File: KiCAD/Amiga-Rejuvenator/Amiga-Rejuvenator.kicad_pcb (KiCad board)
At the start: 4 copper layers, 241.8 x 174.8 mm, 121 parts, among them J1 VIA, J15 28M, J17 RMBCLKS, J18 GND, J19 +12X, U1 74LS245, U10 V53C104, U11 V53C104, U12 V53C104, U13 V53C104, U14 74LS244-U16,U17, U15 74LS373, U16 74LS244-U16,U17, U17 74LS244-U16,U17, U18 512K-ROM, U19 8372-FatAgnus, U19B1 8361-Agnus, U2 74LS393-U2, U20 8364-Paula, U20B1 8364-Paula, U21 74LS245, U22 74LS245, U23 RP, U24 RP, U25 8362-Denise, U25B1 8362-Denise, U26 74HC245, U27 OKI6242B, U28 PAL16L8, U29 PAL16L8, U3 74F257, U30 PAL20L8, U31 PAL20L8, U32 74LS74, U33 74LS04, U34 74HC245, U35 74F257, U36 PALCAS, U37 PALEN, U38 U3I 244, U39 U3G 244, U4 74LS244-U16,U17, U40 U2J F257, U41 U2I F257, U5 74LS373, U6 V53C104, U7 V53C104, U8 V53C104, U9 V53C104, X1 X1, X14 X14, X15 X15, X16 VideoSlot 1, X17 VideoSlot 2, Y1 Crystal

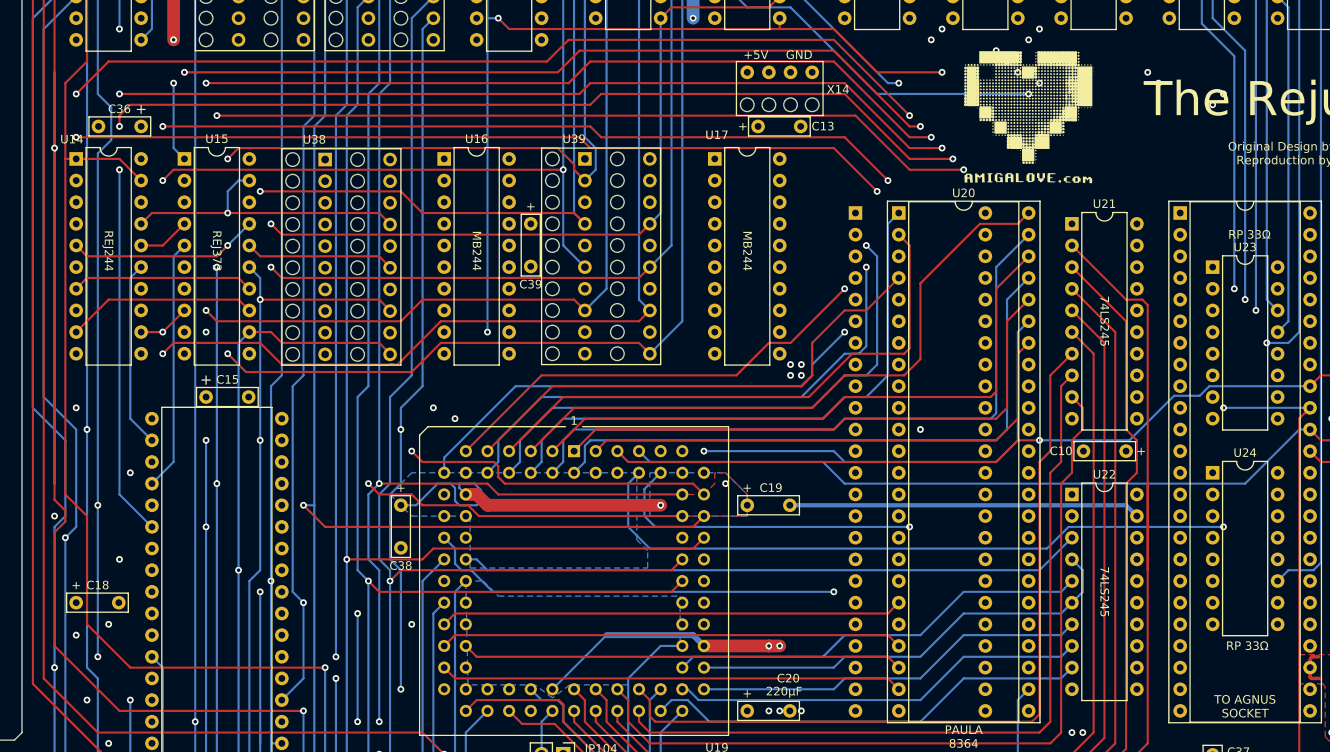
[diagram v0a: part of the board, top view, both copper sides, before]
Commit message: Signal name updates
Signal name updates on KiCAD schematics and board artwork.
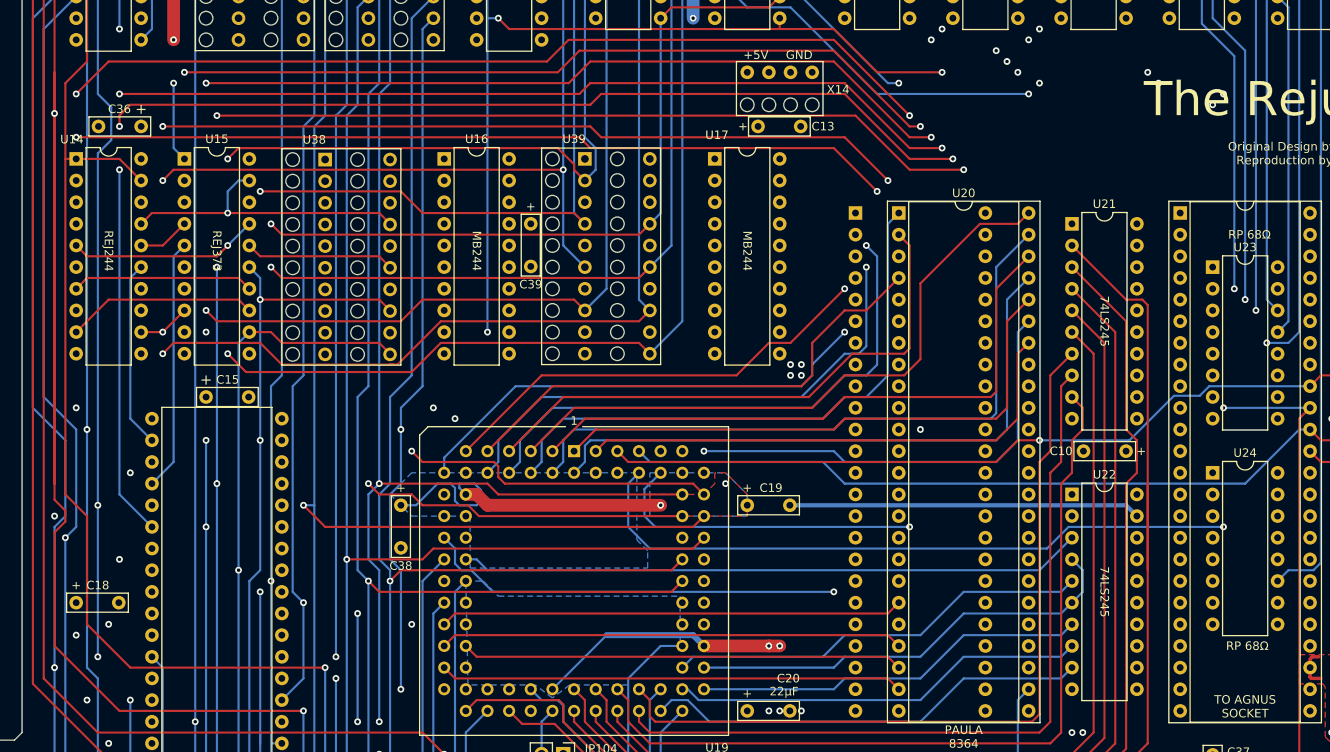
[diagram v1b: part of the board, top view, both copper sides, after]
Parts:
- removed G***: LOGO, rejuvenator_positions:Untitled
- J1: value VIA -> GND
- JP102: value MEM_CONFIG -> JUMPERS
- R10, R11, R12, R6, R7, R9: value 47 -> 33
- U38: value U3I 244 -> U3I
- U39: value U3G 244 -> U3G
- U40: value U2J F257 -> U2J
- U41: value U2I F257 -> U2I
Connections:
- net /REJ.1 renamed /REJ1
- net /REJ.2 renamed /REJ2
- net /REJ.3 renamed /REJ3
- net /REJ.4 renamed /~CNT
- net /REJ.KICK renamed /REJKICK
- net /REJ.MCFG1 renamed /MCFG1
- net /REJ.MCFG2 renamed /MCFG2
- net /REJ.~CE renamed /~DAE
- net /REJ.~OE1 renamed /~CDRREJ
- net /REJ.~OE2 renamed /~CDWREJ
- net /RTC.~RD renamed /~CLKR
- net /RTC.~WR renamed /~CLKW
- net /RW renamed /~PRW
- net /~MYRAME renamed /~ROME
- RP1 pad 10: Net-(RP1-Pad10) -> (no net)
- RP2 pad 10: Net-(RP2-Pad10) -> (no net)
- RP2 pad 9: Net-(RP2-Pad9) -> (no net)
- U19 pad 38: Net-(U19-Pad38) -> (no net)
- U19 pad 39: Net-(U19-Pad39) -> (no net)
- U19B1 pad 1: Net-(U19B1-Pad1) -> (no net)
- U19B1 pad 11: Net-(U19B1-Pad11) -> (no net)
- U19B1 pad 12: Net-(U19B1-Pad12) -> (no net)
- U19B1 pad 13: Net-(U19B1-Pad13) -> (no net)
- U19B1 pad 14: Net-(U19B1-Pad14) -> (no net)
- U19B1 pad 15: Net-(U19B1-Pad15) -> (no net)
- U19B1 pad 16: Net-(U19B1-Pad16) -> (no net)
- U19B1 pad 17: Net-(U19B1-Pad17) -> (no net)
- U19B1 pad 18: Net-(U19B1-Pad18) -> (no net)
- U19B1 pad 19: Net-(U19B1-Pad19) -> (no net)
- U19B1 pad 2: Net-(U19B1-Pad2) -> (no net)
- U19B1 pad 20: Net-(U19B1-Pad20) -> (no net)
- U19B1 pad 21: Net-(U19B1-Pad21) -> (no net)
- U19B1 pad 22: Net-(U19B1-Pad22) -> (no net)
- U19B1 pad 23: Net-(U19B1-Pad23) -> (no net)
- U19B1 pad 24: Net-(U19B1-Pad24) -> (no net)
- U19B1 pad 28: Net-(U19B1-Pad28) -> (no net)
- U19B1 pad 29: Net-(U19B1-Pad29) -> (no net)
- U19B1 pad 3: Net-(U19B1-Pad3) -> (no net)
- U19B1 pad 30: Net-(U19B1-Pad30) -> (no net)
- U19B1 pad 31: Net-(U19B1-Pad31) -> (no net)
- U19B1 pad 32: Net-(U19B1-Pad32) -> (no net)
- U19B1 pad 33: Net-(U19B1-Pad33) -> (no net)
- U19B1 pad 34: Net-(U19B1-Pad34) -> (no net)
- U19B1 pad 35: Net-(U19B1-Pad35) -> (no net)
- U19B1 pad 36: Net-(U19B1-Pad36) -> (no net)
- U19B1 pad 4: Net-(U19B1-Pad4) -> (no net)
- U19B1 pad 41: Net-(U19B1-Pad41) -> (no net)
- U19B1 pad 42: Net-(U19B1-Pad42) -> (no net)
- U19B1 pad 43: Net-(U19B1-Pad43) -> (no net)
- U19B1 pad 44: Net-(U19B1-Pad44) -> (no net)
- U19B1 pad 45: Net-(U19B1-Pad45) -> (no net)
- U19B1 pad 46: Net-(U19B1-Pad46) -> (no net)
- U19B1 pad 47: Net-(U19B1-Pad47) -> (no net)
- U19B1 pad 48: Net-(U19B1-Pad48) -> (no net)
- U19B1 pad 5: Net-(U19B1-Pad5) -> (no net)
- U19B1 pad 6: Net-(U19B1-Pad6) -> (no net)
- U19B1 pad 7: Net-(U19B1-Pad7) -> (no net)
- U19B1 pad 8: Net-(U19B1-Pad8) -> (no net)
- U19B1 pad 9: Net-(U19B1-Pad9) -> (no net)
- U20B1 pad 1: Net-(U20B1-Pad1) -> (no net)
- U20B1 pad 10: Net-(U20B1-Pad10) -> (no net)
- U20B1 pad 19: Net-(U20B1-Pad19) -> (no net)
- U20B1 pad 2: Net-(U20B1-Pad2) -> (no net)
- U20B1 pad 20: Net-(U20B1-Pad20) -> (no net)
- U20B1 pad 21: Net-(U20B1-Pad21) -> (no net)
- U20B1 pad 22: Net-(U20B1-Pad22) -> (no net)
- U20B1 pad 23: Net-(U20B1-Pad23) -> (no net)
- U20B1 pad 24: Net-(U20B1-Pad24) -> (no net)
- U20B1 pad 25: Net-(U20B1-Pad25) -> (no net)
- U20B1 pad 26: Net-(U20B1-Pad26) -> (no net)
- U20B1 pad 3: Net-(U20B1-Pad3) -> (no net)
- U20B1 pad 4: Net-(U20B1-Pad4) -> (no net)
- U20B1 pad 42: Net-(U20B1-Pad42) -> (no net)
- U20B1 pad 43: Net-(U20B1-Pad43) -> (no net)
- U20B1 pad 44: Net-(U20B1-Pad44) -> (no net)
- U20B1 pad 45: Net-(U20B1-Pad45) -> (no net)
- U20B1 pad 46: Net-(U20B1-Pad46) -> (no net)
- U20B1 pad 47: Net-(U20B1-Pad47) -> (no net)
- U20B1 pad 48: Net-(U20B1-Pad48) -> (no net)
- U20B1 pad 5: Net-(U20B1-Pad5) -> (no net)
- U20B1 pad 6: Net-(U20B1-Pad6) -> (no net)
- U20B1 pad 7: Net-(U20B1-Pad7) -> (no net)
- U20B1 pad 9: Net-(U20B1-Pad9) -> (no net)
- U22 pad 2: Net-(U22-Pad2) -> (no net)
- U24 pad 16: Net-(U24-Pad16) -> (no net)
- U25B1 pad 1: Net-(U25B1-Pad1) -> (no net)
- U25B1 pad 10: Net-(U25B1-Pad10) -> (no net)
- U25B1 pad 11: Net-(U25B1-Pad11) -> (no net)
- U25B1 pad 12: Net-(U25B1-Pad12) -> (no net)
- U25B1 pad 13: Net-(U25B1-Pad13) -> (no net)
- U25B1 pad 14: Net-(U25B1-Pad14) -> (no net)
- U25B1 pad 15: Net-(U25B1-Pad15) -> (no net)
- U25B1 pad 16: Net-(U25B1-Pad16) -> (no net)
- U25B1 pad 17: Net-(U25B1-Pad17) -> (no net)
- U25B1 pad 2: Net-(U25B1-Pad2) -> (no net)
- U25B1 pad 3: Net-(U25B1-Pad3) -> (no net)
- U25B1 pad 32: Net-(U25B1-Pad32) -> (no net)
- U25B1 pad 34: Net-(U25B1-Pad34) -> (no net)
- U25B1 pad 4: Net-(U25B1-Pad4) -> (no net)
- U25B1 pad 40: Net-(U25B1-Pad40) -> (no net)
- U25B1 pad 41: Net-(U25B1-Pad41) -> (no net)
- U25B1 pad 42: Net-(U25B1-Pad42) -> (no net)
- U25B1 pad 43: Net-(U25B1-Pad43) -> (no net)
- U25B1 pad 44: Net-(U25B1-Pad44) -> (no net)
- U25B1 pad 45: Net-(U25B1-Pad45) -> (no net)
- U25B1 pad 46: Net-(U25B1-Pad46) -> (no net)
- U25B1 pad 47: Net-(U25B1-Pad47) -> (no net)
- U25B1 pad 48: Net-(U25B1-Pad48) -> (no net)
- U25B1 pad 5: Net-(U25B1-Pad5) -> (no net)
- U25B1 pad 6: Net-(U25B1-Pad6) -> (no net)
- U25B1 pad 7: Net-(U25B1-Pad7) -> (no net)
- U32 pad 6: Net-(U32-Pad6) -> (no net)
- U32 pad 8: Net-(U32-Pad8) -> (no net)
- U34 pad 11: Net-(U34-Pad11) -> (no net)
- U34 pad 12: Net-(U34-Pad12) -> (no net)
- U34 pad 8: Net-(U34-Pad8) -> (no net)
- U34 pad 9: Net-(U34-Pad9) -> (no net)
- X16 pad 1: Net-(X16-Pad1) -> (no net)
- X16 pad 10: Net-(X16-Pad10) -> (no net)
- X16 pad 11: Net-(X16-Pad11) -> (no net)
- X16 pad 15: Net-(X16-Pad15) -> (no net)
- X16 pad 16: Net-(X16-Pad16) -> (no net)
- X16 pad 2: Net-(X16-Pad2) -> (no net)
- X16 pad 28: Net-(X16-Pad28) -> (no net)
- X16 pad 3: Net-(X16-Pad3) -> (no net)
- X16 pad 31: Net-(X16-Pad31) -> (no net)
- X16 pad 33: Net-(X16-Pad33) -> (no net)
- X16 pad 35: Net-(X16-Pad35) -> (no net)
- X16 pad 36: Net-(X16-Pad36) -> (no net)
- X16 pad 4: Net-(X16-Pad4) -> (no net)
- X16 pad 5: Net-(X16-Pad5) -> (no net)
- X16 pad 7: Net-(X16-Pad7) -> (no net)
- X17 pad 13: Net-(X17-Pad13) -> (no net)
- X17 pad 14: Net-(X17-Pad14) -> (no net)
- X17 pad 16: Net-(X17-Pad16) -> (no net)
- X17 pad 18: Net-(X17-Pad18) -> (no net)
- X17 pad 20: Net-(X17-Pad20) -> (no net)
- X17 pad 21: Net-(X17-Pad21) -> (no net)
- X17 pad 23: Net-(X17-Pad23) -> (no net)
- X17 pad 24: Net-(X17-Pad24) -> (no net)
- X17 pad 25: Net-(X17-Pad25) -> (no net)
- X17 pad 26: Net-(X17-Pad26) -> (no net)
- X17 pad 27: Net-(X17-Pad27) -> (no net)
- X17 pad 28: Net-(X17-Pad28) -> (no net)
- X17 pad 29: Net-(X17-Pad29) -> (no net)
- X17 pad 30: Net-(X17-Pad30) -> (no net)
- X17 pad 31: Net-(X17-Pad31) -> (no net)
- X17 pad 33: Net-(X17-Pad33) -> (no net)
- X17 pad 35: Net-(X17-Pad35) -> (no net)
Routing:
- net GND: track 928.7 -> 932.5 mm
- net /~CDRREJ: track 331.2 -> 334.3 mm
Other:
- board text added: "RP 68Ω"
- board text removed: "220µF"
- board text removed: "RP 33Ω"

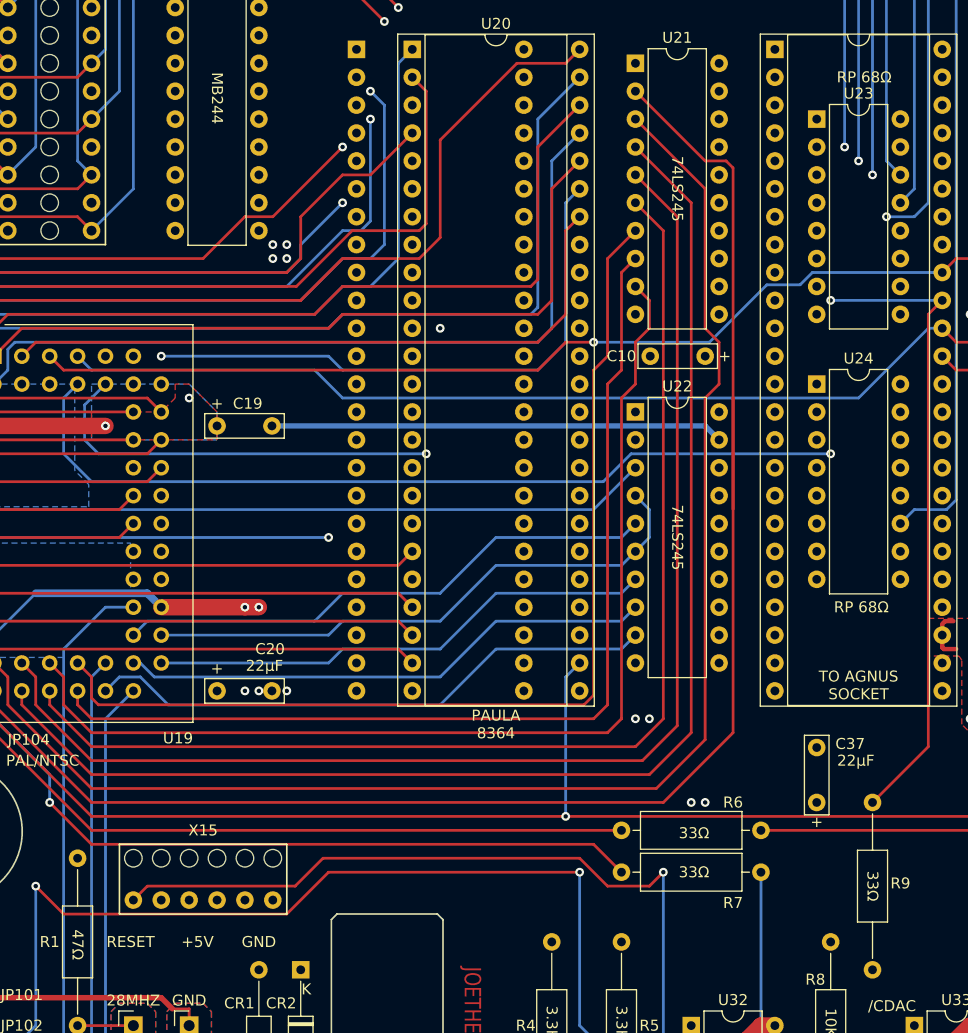
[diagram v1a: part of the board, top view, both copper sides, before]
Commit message: Update board artwork
Rejuvenator board artwork (KiCAD) updated with proper resistor and capacitor values.
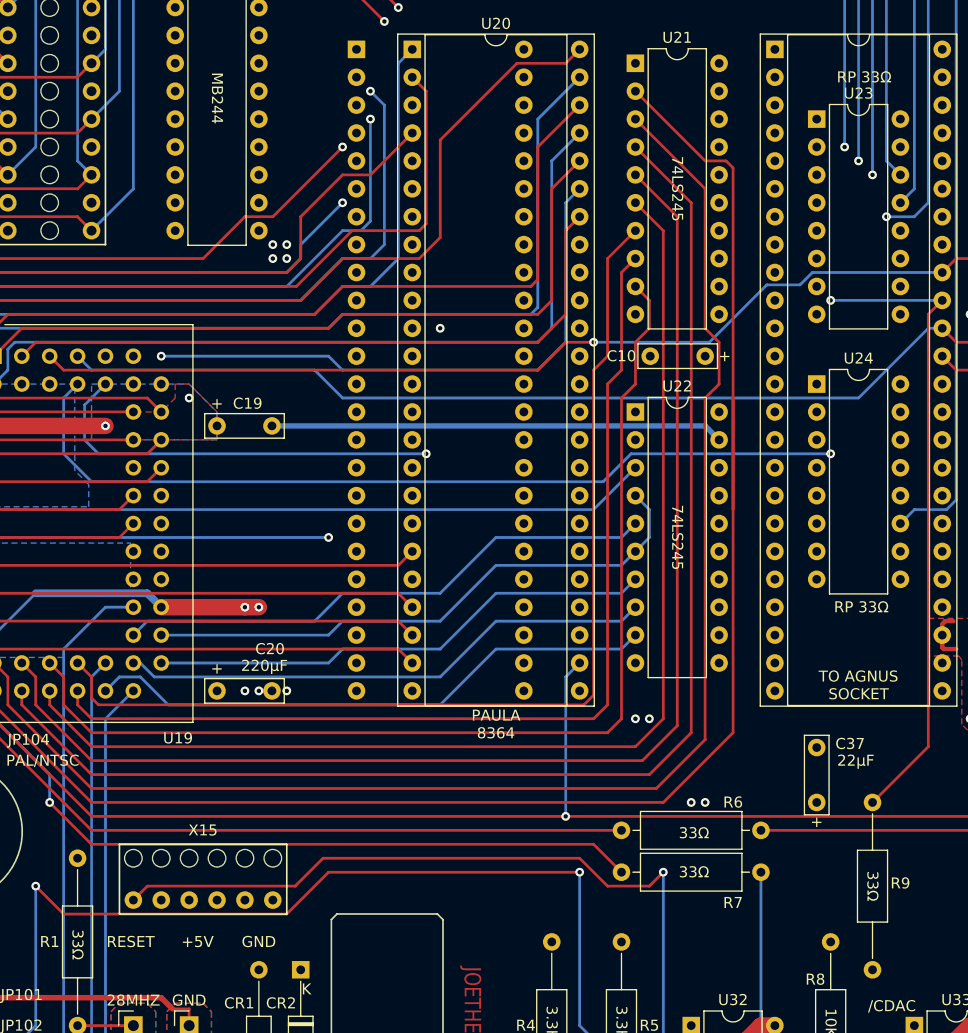
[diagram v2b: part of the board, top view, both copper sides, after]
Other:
- board text added: "220µF"
- board text added: "RP 33Ω"
- board text removed: "47Ω"
- board text removed: "RP 68Ω"

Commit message: Signal names and active low status updated
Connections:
- net /REJ1 renamed /_REJ1
- net /REJ2 renamed /_REJ2
- net /REJ3 renamed /_REJ3

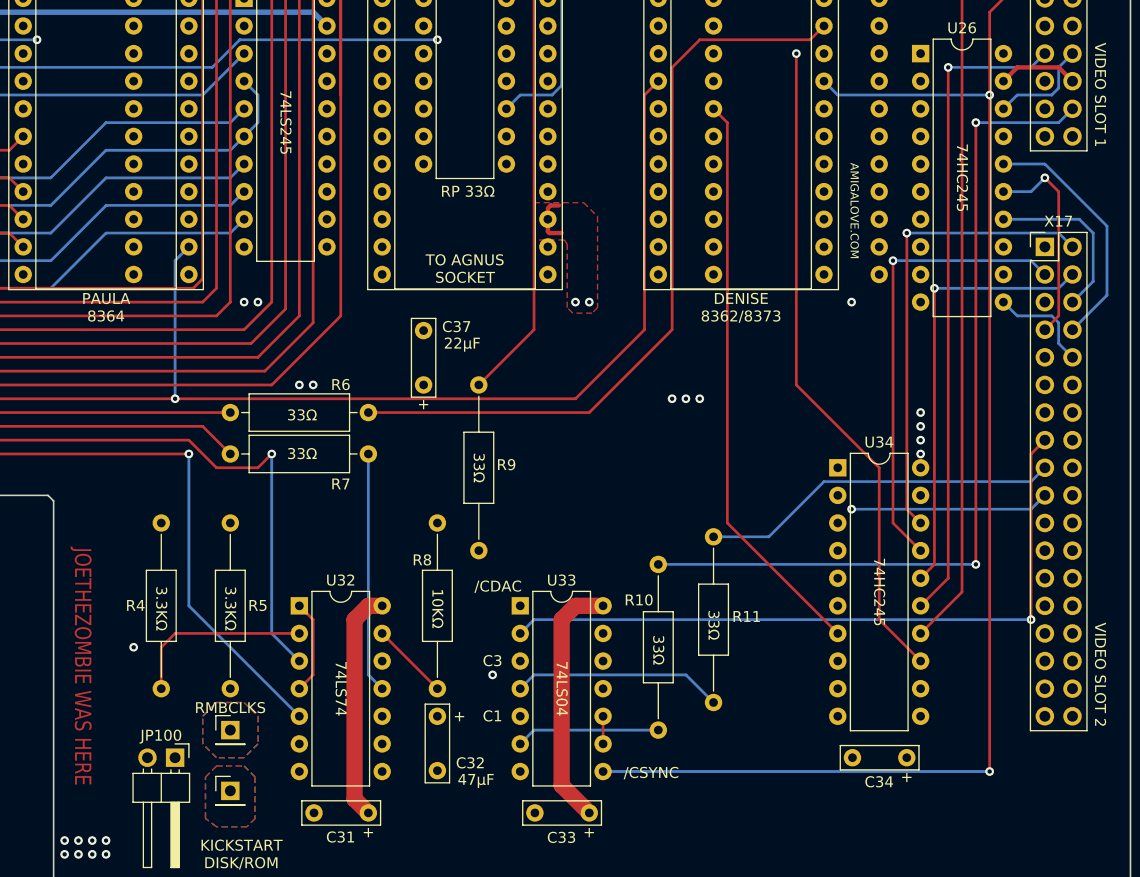
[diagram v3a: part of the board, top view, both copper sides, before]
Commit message: GND trace cleanup
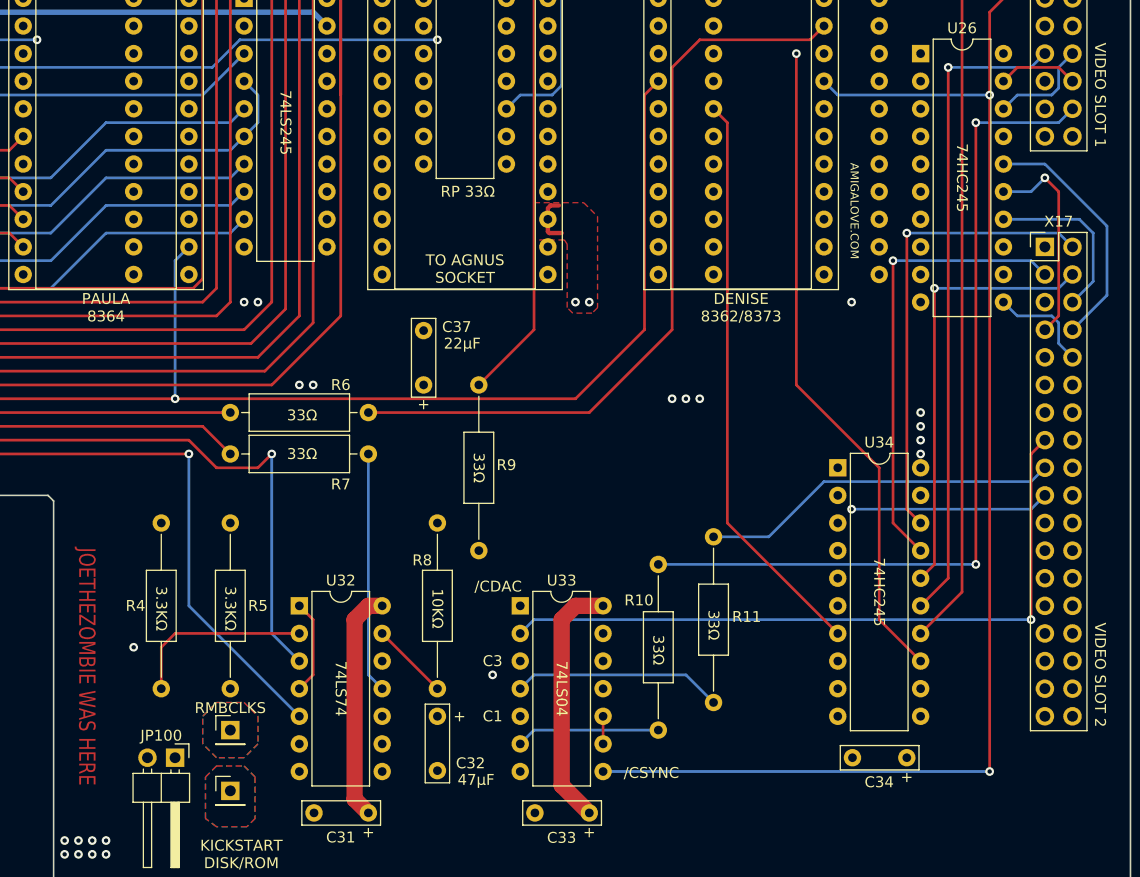
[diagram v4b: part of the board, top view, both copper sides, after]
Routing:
- net GND: track 932.5 -> 629.9 mm
- net +5V: track 528.4 -> 384.1 mm

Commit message: Power plane update
Eliminated redundant tracks placed inside fill zones.
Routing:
- net +5V: track 384.1 -> 383.4 mm
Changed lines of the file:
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@@
     (thickness 1.6)
     (drawings 136)
-    (tracks 3373)
+    (tracks 3372)
     (zones 0)
     (modules 120)
@@
   (segment (start 95.25 186.69) (end 92.71 189.23) (width 0.5) (layer In2.Cu) (net 6))
   (segment (start 92.71 189.23) (end 92.71 194.31) (width 0.5) (layer In2.Cu) (net 6))
-  (segment (start 92.71 194.31) (end 91.44 194.31) (width 0.25) (layer In2.Cu) (net 6))
-  (segment (start 88.9 196.85) (end 88.9 199.39) (width 0.25) (layer In2.Cu) (net 6) (status 20))
-  (segment (start 91.44 194.31) (end 88.9 196.85) (width 0.25) (layer In2.Cu) (net 6))
   (segment (start 128.905 163.195) (end 129.54 162.56) (width 1.5) (layer In2.Cu) (net 6) (status 20))
   (segment (start 121.285 163.195) (end 128.905 163.195) (width 1.5) (layer In2.Cu) (net 6))
@@
   (segment (start 203.2 105.41) (end 203.2 106.68) (width 0.5) (layer In2.Cu) (net 6))
   (segment (start 200.66 102.87) (end 203.2 105.41) (width 0.5) (layer In2.Cu) (net 6))
+  (segment (start 88.9 198.12) (end 92.71 194.31) (width 0.5) (layer In2.Cu) (net 6))
+  (segment (start 88.9 199.39) (end 88.9 198.12) (width 0.5) (layer In2.Cu) (net 6))
   (segment (start 250.19 212.09) (end 247.65 209.55) (width 0.25) (layer In2.Cu) (net 7) (status 10))
   (segment (start 247.65 209.55) (end 242.57 209.55) (width 0.25) (layer In2.Cu) (net 7) (status 20))
